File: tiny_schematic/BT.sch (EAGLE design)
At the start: 2 parts

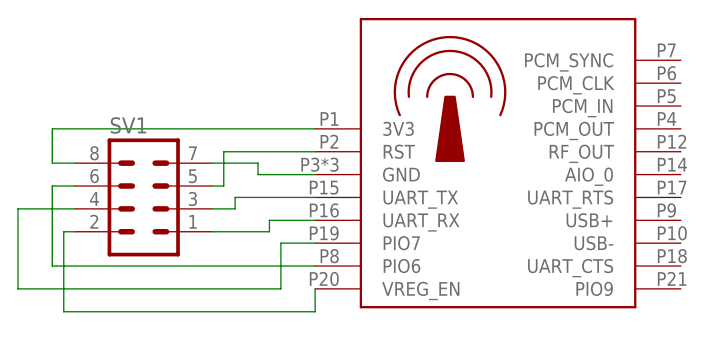
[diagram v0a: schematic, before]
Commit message: BT-Module finished IR-header moved
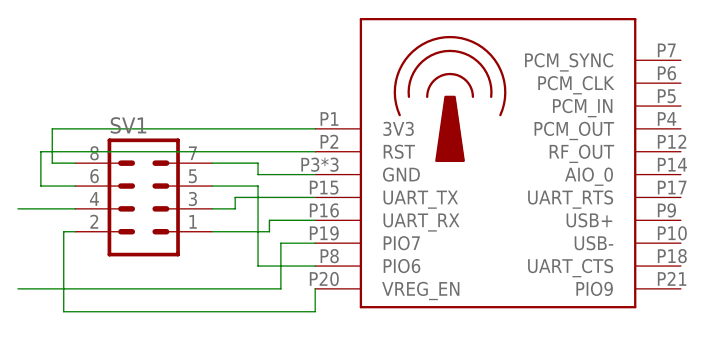
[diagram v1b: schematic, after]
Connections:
- new net N$9: SV1.4
- net N$3: now also SV1.6; no longer SV1.5
- net N$6: now also SV1.5; no longer SV1.6
- net N$7: no longer SV1.4
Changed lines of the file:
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@@
 <setting verticaltext="up"/>
 </settings>
-<grid distance="0.05" unitdist="inch" unit="inch" style="lines" multiple="1" display="no" altdistance="0.025" altunitdist="inch" altunit="inch"/>
+<grid distance="0.1" unitdist="inch" unit="inch" style="lines" multiple="1" display="no" altdistance="0.01" altunitdist="inch" altunit="inch"/>
 <layers>
 <layer number="1" name="Top" color="4" fill="1" visible="no" active="no"/>
@@
 <net name="N$3" class="0">
 <segment>
-<pinref part="SV1" gate="G$1" pin="5"/>
-<wire x1="10.16" y1="22.86" x2="11.43" y2="22.86" width="0.1524" layer="91"/>
-<wire x1="11.43" y1="22.86" x2="11.43" y2="26.67" width="0.1524" layer="91"/>
 <pinref part="BT1" gate="G$1" pin="RST"/>
-<wire x1="11.43" y1="26.67" x2="21.59" y2="26.67" width="0.1524" layer="91"/>
+<wire x1="-8.89" y1="26.67" x2="21.59" y2="26.67" width="0.1524" layer="91"/>
+<wire x1="-8.89" y1="26.67" x2="-8.89" y2="22.86" width="0.1524" layer="91"/>
+<pinref part="SV1" gate="G$1" pin="6"/>
+<wire x1="-8.89" y1="22.86" x2="-5.08" y2="22.86" width="0.1524" layer="91"/>
 </segment>
 </net>
@@
 </segment>
 </net>
-<net name="N$6" class="0">
-<segment>
-<pinref part="SV1" gate="G$1" pin="6"/>
-<wire x1="-5.08" y1="22.86" x2="-7.62" y2="22.86" width="0.1524" layer="91"/>
-<wire x1="-7.62" y1="22.86" x2="-7.62" y2="13.97" width="0.1524" layer="91"/>
-<wire x1="-7.62" y1="13.97" x2="21.59" y2="13.97" width="0.1524" layer="91"/>
-<pinref part="BT1" gate="G$1" pin="PIO6"/>
-</segment>
-</net>
 <net name="N$7" class="0">
 <segment>
-<pinref part="SV1" gate="G$1" pin="4"/>
-<wire x1="-5.08" y1="20.32" x2="-11.43" y2="20.32" width="0.1524" layer="91"/>
-<wire x1="-11.43" y1="20.32" x2="-11.43" y2="11.43" width="0.1524" layer="91"/>
 <wire x1="-11.43" y1="11.43" x2="17.78" y2="11.43" width="0.1524" layer="91"/>
 <wire x1="17.78" y1="11.43" x2="17.78" y2="16.51" width="0.1524" layer="91"/>
@@
 <net name="N$8" class="0">
 <segment>
-<pinref part="SV1" gate="G$1" pin="2"/>
-<wire x1="-5.08" y1="17.78" x2="-6.35" y2="17.78" width="0.1524" layer="91"/>
 <wire x1="-6.35" y1="17.78" x2="-6.35" y2="8.89" width="0.1524" layer="91"/>
 <pinref part="BT1" gate="G$1" pin="VREG_EN"/>
 <wire x1="-6.35" y1="8.89" x2="21.59" y2="8.89" width="0.1524" layer="91"/>
 <wire x1="21.59" y1="8.89" x2="21.59" y2="11.43" width="0.1524" layer="91"/>
-</segment>
-</net>
+<pinref part="SV1" gate="G$1" pin="2"/>
+<wire x1="-6.35" y1="17.78" x2="-5.08" y2="17.78" width="0.1524" layer="91"/>
+</segment>
+</net>
+<net name="N$6" class="0">
+<segment>
+<pinref part="SV1" gate="G$1" pin="5"/>
+<wire x1="10.16" y1="22.86" x2="15.24" y2="22.86" width="0.1524" layer="91"/>
+<wire x1="15.24" y1="22.86" x2="15.24" y2="13.97" width="0.1524" layer="91"/>
+<pinref part="BT1" gate="G$1" pin="PIO6"/>
+<wire x1="15.24" y1="13.97" x2="21.59" y2="13.97" width="0.1524" layer="91"/>
+</segment>
+</net>
+<net name="N$9" class="0">
+<segment>
+<pinref part="SV1" gate="G$1" pin="4"/>
+<wire x1="-5.08" y1="20.32" x2="-11.43" y2="20.32" width="0.1524" layer="91"/>
+</segment>
+</net>

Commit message: BT implemented
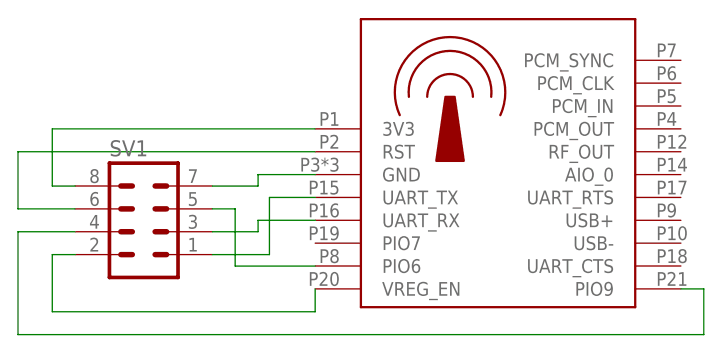
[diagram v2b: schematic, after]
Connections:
- removed net N$9: SV1.4
- net N$1: now also BT1.UART_RX; no longer BT1.UART_TX
- net N$2: now also BT1.UART_TX; no longer BT1.UART_RX
- net N$7: now also BT1.PIO9, SV1.4; no longer BT1.PIO7
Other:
- moved on the sheet: SV1
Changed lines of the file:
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@@
 <setting verticaltext="up"/>
 </settings>
-<grid distance="0.1" unitdist="inch" unit="inch" style="lines" multiple="1" display="no" altdistance="0.01" altunitdist="inch" altunit="inch"/>
+<grid distance="50" unitdist="mil" unit="mil" style="lines" multiple="1" display="no" altdistance="0.01" altunitdist="inch" altunit="inch"/>
 <layers>
 <layer number="1" name="Top" color="4" fill="1" visible="no" active="no"/>
@@
 </plain>
 <instances>
-<instance part="SV1" gate="G$1" x="2.54" y="22.86"/>
+<instance part="SV1" gate="G$1" x="2.54" y="20.32"/>
 <instance part="BT1" gate="G$1" x="21.59" y="11.43"/>
 </instances>
@@
 <net name="N$1" class="0">
 <segment>
+<pinref part="SV1" gate="G$1" pin="3"/>
+<wire x1="15.24" y1="17.78" x2="10.16" y2="17.78" width="0.1524" layer="91"/>
+<wire x1="15.24" y1="17.78" x2="15.24" y2="19.05" width="0.1524" layer="91"/>
+<pinref part="BT1" gate="G$1" pin="UART_RX"/>
+<wire x1="15.24" y1="19.05" x2="21.59" y2="19.05" width="0.1524" layer="91"/>
+</segment>
+</net>
+<net name="N$2" class="0">
+<segment>
+<pinref part="SV1" gate="G$1" pin="1"/>
+<wire x1="10.16" y1="15.24" x2="16.51" y2="15.24" width="0.1524" layer="91"/>
+<wire x1="16.51" y1="15.24" x2="16.51" y2="21.59" width="0.1524" layer="91"/>
 <pinref part="BT1" gate="G$1" pin="UART_TX"/>
-<wire x1="21.59" y1="21.59" x2="12.7" y2="21.59" width="0.1524" layer="91"/>
-<wire x1="12.7" y1="21.59" x2="12.7" y2="20.32" width="0.1524" layer="91"/>
-<pinref part="SV1" gate="G$1" pin="3"/>
-<wire x1="12.7" y1="20.32" x2="10.16" y2="20.32" width="0.1524" layer="91"/>
-</segment>
-</net>
-<net name="N$2" class="0">
-<segment>
-<pinref part="SV1" gate="G$1" pin="1"/>
-<wire x1="10.16" y1="17.78" x2="16.51" y2="17.78" width="0.1524" layer="91"/>
-<wire x1="16.51" y1="17.78" x2="16.51" y2="19.05" width="0.1524" layer="91"/>
-<pinref part="BT1" gate="G$1" pin="UART_RX"/>
-<wire x1="16.51" y1="19.05" x2="21.59" y2="19.05" width="0.1524" layer="91"/>
+<wire x1="16.51" y1="21.59" x2="21.59" y2="21.59" width="0.1524" layer="91"/>
 </segment>
 </net>
@@
 <segment>
 <pinref part="BT1" gate="G$1" pin="RST"/>
-<wire x1="-8.89" y1="26.67" x2="21.59" y2="26.67" width="0.1524" layer="91"/>
-<wire x1="-8.89" y1="26.67" x2="-8.89" y2="22.86" width="0.1524" layer="91"/>
+<wire x1="-11.43" y1="26.67" x2="21.59" y2="26.67" width="0.1524" layer="91"/>
+<wire x1="-11.43" y1="26.67" x2="-11.43" y2="20.32" width="0.1524" layer="91"/>
 <pinref part="SV1" gate="G$1" pin="6"/>
-<wire x1="-8.89" y1="22.86" x2="-5.08" y2="22.86" width="0.1524" layer="91"/>
+<wire x1="-11.43" y1="20.32" x2="-5.08" y2="20.32" width="0.1524" layer="91"/>
 </segment>
 </net>
@@
 <pinref part="SV1" gate="G$1" pin="7"/>
 <pinref part="BT1" gate="G$1" pin="GND"/>
-<wire x1="10.16" y1="25.4" x2="15.24" y2="25.4" width="0.1524" layer="91"/>
-<wire x1="15.24" y1="25.4" x2="15.24" y2="24.13" width="0.1524" layer="91"/>
+<wire x1="10.16" y1="22.86" x2="15.24" y2="22.86" width="0.1524" layer="91"/>
+<wire x1="15.24" y1="22.86" x2="15.24" y2="24.13" width="0.1524" layer="91"/>
 <wire x1="15.24" y1="24.13" x2="21.59" y2="24.13" width="0.1524" layer="91"/>
 </segment>
@@
 <segment>
 <pinref part="SV1" gate="G$1" pin="8"/>
-<wire x1="-5.08" y1="25.4" x2="-7.62" y2="25.4" width="0.1524" layer="91"/>
-<wire x1="-7.62" y1="25.4" x2="-7.62" y2="29.21" width="0.1524" layer="91"/>
+<wire x1="-5.08" y1="22.86" x2="-7.62" y2="22.86" width="0.1524" layer="91"/>
+<wire x1="-7.62" y1="22.86" x2="-7.62" y2="29.21" width="0.1524" layer="91"/>
 <pinref part="BT1" gate="G$1" pin="3V3"/>
 <wire x1="-7.62" y1="29.21" x2="21.59" y2="29.21" width="0.1524" layer="91"/>
 </segment>
 </net>
-<net name="N$7" class="0">
-<segment>
-<wire x1="-11.43" y1="11.43" x2="17.78" y2="11.43" width="0.1524" layer="91"/>
-<wire x1="17.78" y1="11.43" x2="17.78" y2="16.51" width="0.1524" layer="91"/>
-<pinref part="BT1" gate="G$1" pin="PIO7"/>
-<wire x1="17.78" y1="16.51" x2="21.59" y2="16.51" width="0.1524" layer="91"/>
-</segment>
-</net>
 <net name="N$8" class="0">
 <segment>
-<wire x1="-6.35" y1="17.78" x2="-6.35" y2="8.89" width="0.1524" layer="91"/>
+<wire x1="-7.62" y1="15.24" x2="-7.62" y2="8.89" width="0.1524" layer="91"/>
 <pinref part="BT1" gate="G$1" pin="VREG_EN"/>
-<wire x1="-6.35" y1="8.89" x2="21.59" y2="8.89" width="0.1524" layer="91"/>
+<wire x1="-7.62" y1="8.89" x2="21.59" y2="8.89" width="0.1524" layer="91"/>
 <wire x1="21.59" y1="8.89" x2="21.59" y2="11.43" width="0.1524" layer="91"/>
 <pinref part="SV1" gate="G$1" pin="2"/>
-<wire x1="-6.35" y1="17.78" x2="-5.08" y2="17.78" width="0.1524" layer="91"/>
+<wire x1="-7.62" y1="15.24" x2="-5.08" y2="15.24" width="0.1524" layer="91"/>
 </segment>
 </net>
@@
 <segment>
 <pinref part="SV1" gate="G$1" pin="5"/>
-<wire x1="10.16" y1="22.86" x2="15.24" y2="22.86" width="0.1524" layer="91"/>
-<wire x1="15.24" y1="22.86" x2="15.24" y2="13.97" width="0.1524" layer="91"/>
+<wire x1="10.16" y1="20.32" x2="12.7" y2="20.32" width="0.1524" layer="91"/>
+<wire x1="12.7" y1="20.32" x2="12.7" y2="13.97" width="0.1524" layer="91"/>
 <pinref part="BT1" gate="G$1" pin="PIO6"/>
-<wire x1="15.24" y1="13.97" x2="21.59" y2="13.97" width="0.1524" layer="91"/>
-</segment>
-</net>
-<net name="N$9" class="0">
-<segment>
+<wire x1="12.7" y1="13.97" x2="21.59" y2="13.97" width="0.1524" layer="91"/>
+</segment>
+</net>
+<net name="N$7" class="0">
+<segment>
+<pinref part="BT1" gate="G$1" pin="PIO9"/>
+<wire x1="64.77" y1="6.35" x2="64.77" y2="11.43" width="0.1524" layer="91"/>
+<wire x1="64.77" y1="11.43" x2="62.23" y2="11.43" width="0.1524" layer="91"/>
 <pinref part="SV1" gate="G$1" pin="4"/>
-<wire x1="-5.08" y1="20.32" x2="-11.43" y2="20.32" width="0.1524" layer="91"/>
-</segment>
-</net>
+<wire x1="-5.08" y1="17.78" x2="-11.43" y2="17.78" width="0.1524" layer="91"/>
+<wire x1="-11.43" y1="17.78" x2="-11.43" y2="6.35" width="0.1524" layer="91"/>
+<wire x1="-11.43" y1="6.35" x2="64.77" y2="6.35" width="0.1524" layer="91"/>
+</segment>
+</net>

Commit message: BT-layout changed, sleeping status value implemented, IR-alpha implemented
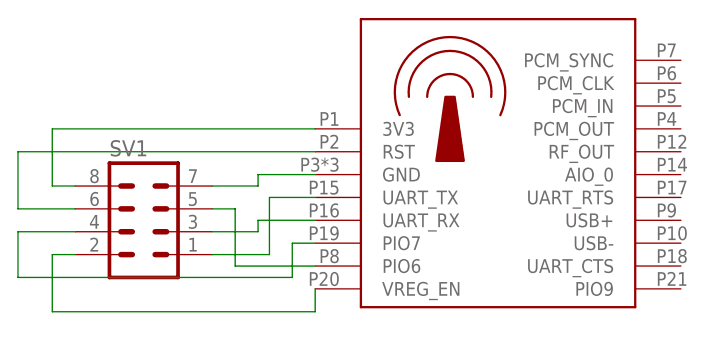
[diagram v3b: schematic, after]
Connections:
- net N$7: now also BT1.PIO7; no longer BT1.PIO9
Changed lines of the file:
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@@
 <net name="N$7" class="0">
 <segment>
-<pinref part="BT1" gate="G$1" pin="PIO9"/>
-<wire x1="64.77" y1="6.35" x2="64.77" y2="11.43" width="0.1524" layer="91"/>
-<wire x1="64.77" y1="11.43" x2="62.23" y2="11.43" width="0.1524" layer="91"/>
 <pinref part="SV1" gate="G$1" pin="4"/>
 <wire x1="-5.08" y1="17.78" x2="-11.43" y2="17.78" width="0.1524" layer="91"/>
-<wire x1="-11.43" y1="17.78" x2="-11.43" y2="6.35" width="0.1524" layer="91"/>
-<wire x1="-11.43" y1="6.35" x2="64.77" y2="6.35" width="0.1524" layer="91"/>
+<wire x1="-11.43" y1="17.78" x2="-11.43" y2="12.7" width="0.1524" layer="91"/>
+<wire x1="-11.43" y1="12.7" x2="19.05" y2="12.7" width="0.1524" layer="91"/>
+<wire x1="19.05" y1="12.7" x2="19.05" y2="16.51" width="0.1524" layer="91"/>
+<pinref part="BT1" gate="G$1" pin="PIO7"/>
+<wire x1="19.05" y1="16.51" x2="21.59" y2="16.51" width="0.1524" layer="91"/>
 </segment>
 </net>
